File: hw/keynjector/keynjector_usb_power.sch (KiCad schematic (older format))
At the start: 7 parts, among them J1 10118192-0001LF, U1 PRTR5V0U2X, U2 SPX3819M5-L/TR

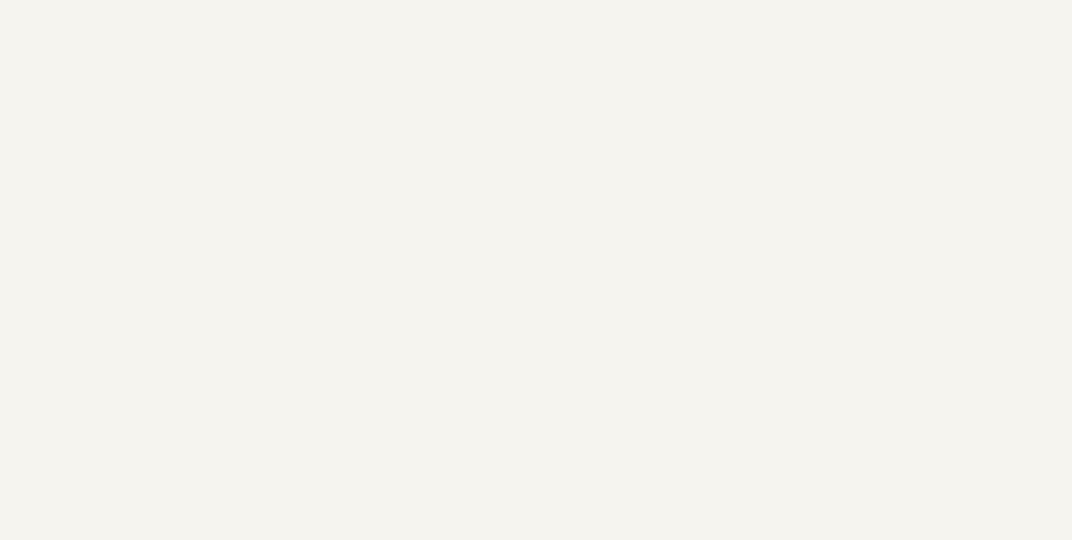
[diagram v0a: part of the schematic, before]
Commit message: added license text to KiCad sheets
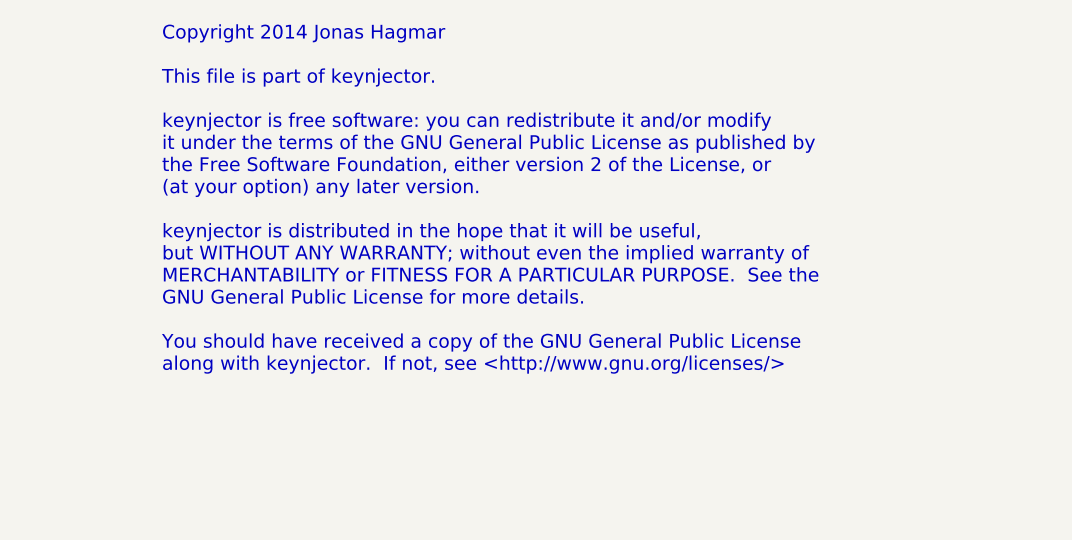
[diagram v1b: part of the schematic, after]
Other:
- note added: "Copyright 2014 Jonas Hagmar\n\nThis file is part of keynjector.\n\nkeynjector is free software: you can redistribute it and/or modify\nit under the terms of the GNU General Public License as published by\nthe Free Software Foundation, either version 2 of the License, or\n(at your option) any later version.\n\nkeynjector is distributed in the hope that it will be useful,\nbut WITHOUT ANY WARRANTY;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"
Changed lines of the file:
@@
 Sheet 2 7
 Title ""
-Date "6 nov 2014"
+Date "2 dec 2014"
 Rev ""
 Comp ""
@@
 	4150 2750 4150 3000
 Connection ~ 4150 3000
+Text Notes 7700 800  0    60   ~ 0
+Copyright 2014 Jonas Hagmar\n\nThis file is part of keynjector.\n\nkeynjector is free software: you can redistribute it and/or modify\nit under the terms of the GNU General Public License as published by\nthe Free Software Foundation, either version 2 of the License, or\n(at your option) any later version.\n\nkeynjector is distributed in the hope that it will be useful,\nbut WITHOUT ANY WARRANTY; without even the implied warranty of\nMERCHANTABILITY or FITNESS FOR A PARTICULAR PURPOSE.  See the\nGNU General Public License for more details.\n\nYou should have received a copy of the GNU General Public License\nalong with keynjector.  If not, see <http://www.gnu.org/licenses/>
 $EndSCHEMATC
